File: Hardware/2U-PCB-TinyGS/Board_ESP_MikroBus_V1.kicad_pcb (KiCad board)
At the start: 2 copper layers, 90 x 92 mm, 21 parts, among them J1 Conn_01x19, J2 Conn_01x19, J3 Bus Standard, U1 ESP32-DEVKITC-32D

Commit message: Design changed
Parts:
- removed the 3.3 at (83.2, 21.6)
- removed the G*** at (20.2, 99.9)
- removed the G*** at (82.9, 64.9)
- removed the G*** at (70.2, 51.4) (x2)
- removed the G*** at (82.7, 64.9)
- removed the G*** at (20.2, 100.7)
- added 3.3: Conn_01x02, Connector_PinHeader_2.54mm:PinHeader_1x02_P2.54mm_Vertical, F.Cu at (79.1, 62.9)
- added 3.3: Conn_01x02, Connector_PinHeader_2.54mm:PinHeader_1x02_P2.54mm_Vertical, F.Cu at (86.7, 62.9)
- added 3.3: Conn_01x02, Connector_PinHeader_2.54mm:PinHeader_1x02_P2.54mm_Vertical, F.Cu at (21.1, 63.4)
- added 3.3: Conn_01x02, Connector_PinHeader_2.54mm:PinHeader_1x02_P2.54mm_Vertical, F.Cu at (82.9, 62.9)
- added 3.3: Conn_01x02, Connector_PinHeader_2.54mm:PinHeader_1x02_P2.54mm_Vertical, F.Cu at (29.2, 63.4)
- added 3.3: Conn_01x02, Connector_PinHeader_2.54mm:PinHeader_1x02_P2.54mm_Vertical, F.Cu at (25.4, 63.4)
- added G***: LOGO, Logos-image:QRCode_ThingSat_14.5x14.5, F.Cu at (96.9, 25.8)
- added G***: LOGO, Logos-image:Image-Csug_10x10, F.Cu at (97.4, 95.4)
- added I2C2: Grove, Connector:NS-Tech_Grove_1x04_P2mm_Vertical, F.Cu at (28.9, 81.4)
- added I2C3: Grove, Connector:NS-Tech_Grove_1x04_P2mm_Vertical, F.Cu at (28.9, 89.3)
- added I2C4: Grove, Connector:NS-Tech_Grove_1x04_P2mm_Vertical, F.Cu at (60.1, 81.4)
- added I2C5: Grove, Connector:NS-Tech_Grove_1x04_P2mm_Vertical, F.Cu at (60.1, 73.5)
- added REF**: MountingHole_3.5mm, MountingHole:MountingHole_3.5mm, F.Cu at (21.5, 19.7)
- added REF**: MountingHole_3.5mm, MountingHole:MountingHole_3.5mm, F.Cu at (21.5, 102.2)
- C2: moved to F.Cu
- moved IO_32/33 67.7 mm to (83.2, 92.6)
- moved I2C1 64.3 mm to (28.9, 73.5)
- moved J2 52.5 mm to (73.2, 56.0), turned to -90 degrees
- moved 5V1 47.8 mm to (44.8, 62.2)
- moved J1 47.4 mm to (73.3, 20.4), turned to -90 degrees
- moved UART0 40.8 mm to (60.1, 89.3), turned to 90 degrees
- moved C1 38.9 mm to (24.0, 27.8), turned to -90 degrees
- moved C2 32.9 mm to (22.7, 24.8), turned to 180 degrees
- moved Jmp_Rx1 28.5 mm to (70.7, 100.5)
- moved Jmp_Tx1 26.5 mm to (61.6, 100.5), turned to -90 degrees
- moved U1 15.4 mm to (53.5, 38.2), turned to -90 degrees
- moved MiKroBus_1 10.8 mm to (73.8, 88.1), turned to 180 degrees
- moved MiKroBus_0 10.7 mm to (43.3, 88.1), turned to 180 degrees
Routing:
- net I2C_SDA: track 236.2 -> 126.4 mm, vias 1 -> 2
- net I2C_SCL: track 232.6 -> 142.7 mm, vias 0 -> 1
- net PWM_1: track 112.8 -> 50.9 mm, vias 2 -> 1
- net UART2_Tx: track 116.9 -> 60.4 mm
- net Reset_1: track 59.9 -> 106.4 mm
- net UART0_Tx: track 78.1 -> 36.0 mm, vias 0 -> 1
- net UART0_Rx: track 78.1 -> 36.2 mm
- net AN_0: track 40.5 -> 78.2 mm
- net Reset_0: track 42.2 -> 78.0 mm, vias 0 -> 1
- net /13: track 45.5 -> 77.0 mm, vias 0 -> 1
- net AN_1: track 59.8 -> 90.1 mm
- net PWM_0: track 66.7 -> 93.4 mm, vias 0 -> 2
- net /34: track 90.1 -> 66.0 mm
- net MISO_0: track 81.4 -> 57.3 mm
- net UART2_Rx_grove: track 48.1 -> 25.1 mm, vias 1 -> 0
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- added copper zone on B.Cu, net +3.3V
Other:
- board text added: "TinyGS_2.4GHz_Station"
- board text added: "TinyGS_2U_Board_V1"
- board text removed: "Board_V1"
- board text removed: "Board_V1-2U FORMAT"
- board text removed: "ESP32"
- board text removed: "TinyGs_2.4GHz"

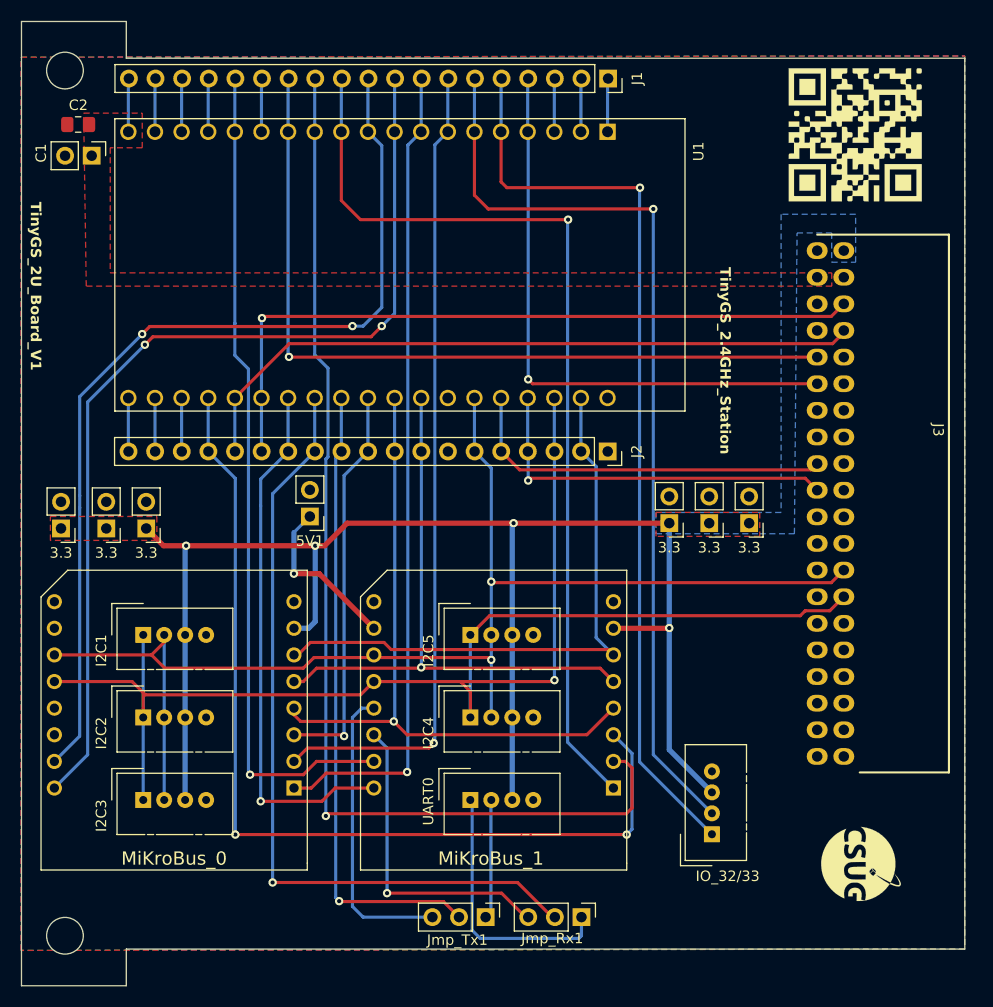
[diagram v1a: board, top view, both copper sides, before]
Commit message: Selection CAN juper added. Can buffer added
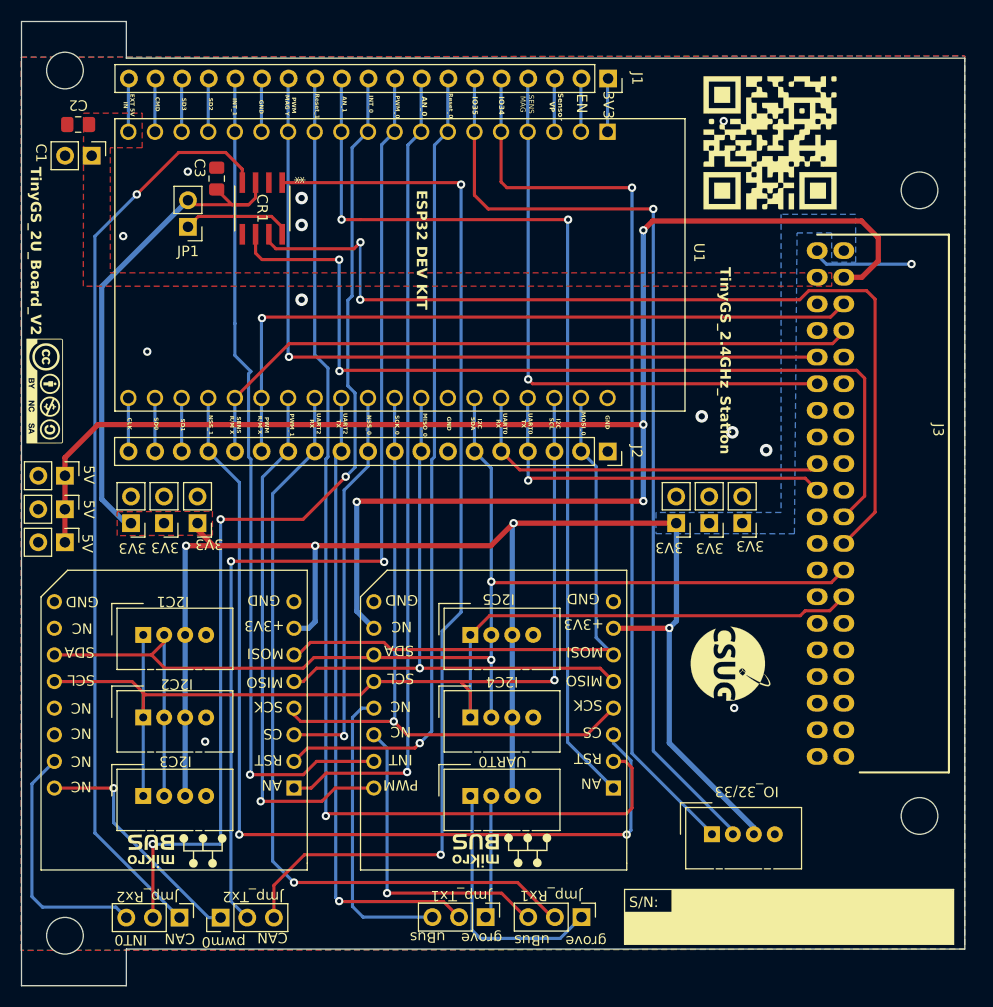
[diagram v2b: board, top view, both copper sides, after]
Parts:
- added 5V1: Conn_01x02, Connector_PinHeader_2.54mm:PinHeader_1x02_P2.54mm_Vertical, F.Cu at (21.5, 58.3)
- added 5V2: Conn_01x02, Connector_PinHeader_2.54mm:PinHeader_1x02_P2.54mm_Vertical, F.Cu at (21.5, 61.5)
- added C3: 100nF, Capacitor_SMD:C_0805_2012Metric_Pad1.18x1.45mm_HandSolder, F.Cu at (35.9, 30.0)
- added CR1: L9616, CAN_buffer:SO-8_STM, F.Cu at (40.3, 32.8)
- added G***: LOGO, Logos-image:mikrobus_logo, F.Cu at (32.4, 94.2)
- added G***: LOGO, Logos-image:mikrobus_logo, F.Cu at (63.4, 94.2)
- added G***: LOGO, Logos-image:license_cc_by_nc_sa, F.Cu at (19.5, 50.3)
- added JP1: Jumper_2_Open, Connector_PinHeader_2.54mm:PinHeader_1x02_P2.54mm_Vertical, F.Cu at (33.2, 34.6)
- added Jmp_Rx2: Jumper_NC_Dual, Connector_PinHeader_2.54mm:PinHeader_1x03_P2.54mm_Vertical, F.Cu at (32.4, 100.5)
- added Jmp_Tx2: Jumper_NC_Dual, Connector_PinHeader_2.54mm:PinHeader_1x03_P2.54mm_Vertical, F.Cu at (36.3, 100.5)
- added REF**: MountingHole_3.5mm, MountingHole:MountingHole_3.5mm, F.Cu at (103.0, 31.1)
- added REF**: MountingHole_3.5mm, MountingHole:MountingHole_3.5mm, F.Cu at (103.0, 90.8)
- moved 5V3 23.5 mm to (21.5, 64.7), turned to -90 degrees
- moved G*** 22.8 mm to (85.0, 76.3)
- moved G*** 8.16 mm to (88.8, 26.5)
- moved 3.1 6.69 mm to (27.8, 62.9)
- moved 3.2 5.53 mm to (30.9, 62.9)
- moved 3.3 4.92 mm to (34.1, 62.9)
- moved 3.4 0.66 mm to (79.8, 62.9)
- moved 3.6 0.66 mm to (86.1, 62.9)
- moved I2C3 0.38 mm to (28.9, 88.9)
- moved UART0 0.38 mm to (60.1, 88.9)
- turned IO_32/33 to 90 degrees
- renumbered 3.3 to 3.1, 3.3 to 3.2, 3.3 to 3.4, 3.3 to 3.5, 3.3 to 3.6, 5V1 to 5V3
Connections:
- J1 pad 10: INT_0 -> ESP_CAN0_RD/INT_0
- J1 pad 9: PWM_0 -> ESP_CAN0_TD/PWM_0
- J3 pad 22: unconnected-(J3-RD-Pad22) -> CAN_RD
- J3 pad 24: unconnected-(J3-TD-Pad24) -> CAN_TD
- J3 pad 4: unconnected-(J3-5V-Pad4) -> +5V
- U1 pad 10: INT_0 -> ESP_CAN0_RD/INT_0
- U1 pad 9: PWM_0 -> ESP_CAN0_TD/PWM_0
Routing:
- net +5V: track 15.9 -> 160.1 mm, vias 1 -> 4
- net CAN0_TD: track 0.00 -> 102.1 mm, vias 0 -> 2
- net ESP_CAN0_RD/INT_0: track 0.00 -> 97.6 mm, vias 0 -> 3
- net ESP_CAN0_TD/PWM_0: track 0.00 -> 96.0 mm, vias 0 -> 2
- net CAN_TD: track 0.00 -> 89.8 mm, vias 0 -> 2
- net CAN0_RD: track 0.00 -> 87.7 mm, vias 0 -> 1
- net CAN_RD: track 0.00 -> 85.2 mm, vias 0 -> 2
- net PWM_0: track 93.4 -> 22.9 mm, vias 2 -> 1
- net INT_0: track 90.6 -> 23.6 mm, vias 2 -> 0
- net +3.3V: track 144.5 -> 196.3 mm
- net Net-(CR1-ASC): track 0.00 -> 10.9 mm
- net GNDREF: track 5.10 -> 14.9 mm, vias 0 -> 13
- net IN35: track 88.7 -> 91.6 mm
- net UART2_Rx: track 76.2 -> 75.0 mm
- net AN_1: track 90.1 -> 91.2 mm, vias 1 -> 2
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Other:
- board text added: "+3V3"
- board text added: "3V3"
- board text added: "5V"
- board text added: "AN"
- board text added: "AN_0"
- board text added: "AN_1"
- board text added: "CAN"
- board text added: "CLK"
- board text added: "CMD"
- board text added: "CS"
- board text added: "EN"
- board text added: "ESP32 DEV KIT"
- board text added: "EXT 5V IN"
- board text added: "GND"
- board text added: "I2C SCL"
- board text added: "I2C SDA"
- board text added: "INT"
- board text added: "INT0"
- board text added: "INT_0"
- board text added: "INT_1"
- board text added: "IO34"
- board text added: "IO35"
- board text added: "MISO"
- board text added: "MISO_0"
- board text added: "MOSI"
- board text added: "MOSI_0"
- board text added: "NC"
- board text added: "NSS_0"
- board text added: "NSS_1"
- board text added: "PWM"
- board text added: "PWM MAG Y"
- board text added: "PWM R/M X"
- board text added: "PWM_0"
- board text added: "PWM_1"
- board text added: "RST"
- board text added: "Reset_0"
- board text added: "Reset_1"
- board text added: "S/N:"
- board text added: "SCK"
- board text added: "SCK_0"
- board text added: "SCL"
- board text added: "SD0"
- board text added: "SD1"
- board text added: "SD2"
- board text added: "SD3"
- board text added: "SDA"
- board text added: "SENS MAG"
- board text added: "SENS R/M X"
- board text added: "Sensor VP"
- board text added: "TinyGS_2U_Board_V2"
- board text added: "UART0 RX"
- board text added: "UART0 TX"
- board text added: "UART2 RX"
- board text added: "UART2 TX"
- board text added: "grove"
- board text added: "pwm0"
- board text added: "uBus"
- board text removed: "TinyGS_2U_Board_V1"

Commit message: Flatsat connector was in the wrong side. All routes were remade.
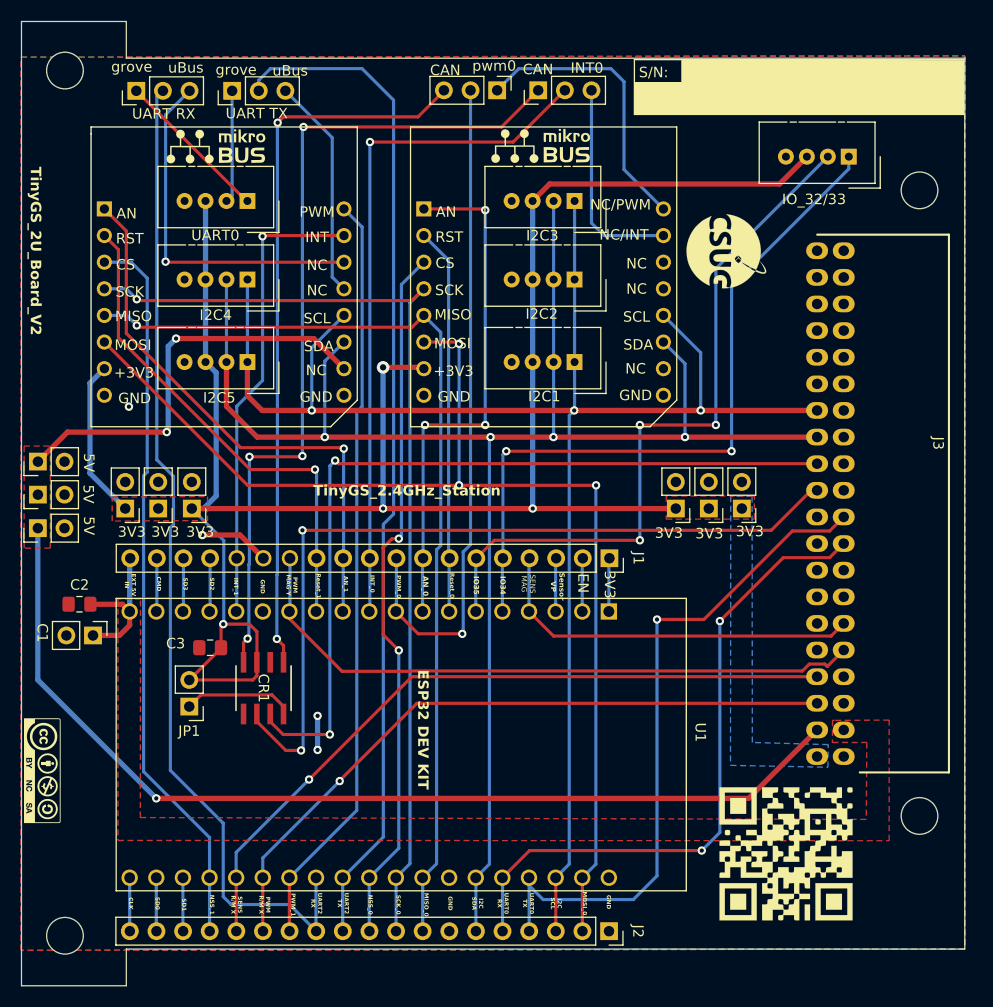
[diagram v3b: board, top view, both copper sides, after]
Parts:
- moved Jmp_Rx1 89.6 mm to (28.3, 21.6), turned to 90 degrees
- moved Jmp_Rx2 86.0 mm to (66.6, 21.6), turned to 90 degrees
- moved Jmp_Tx2 83.2 mm to (62.7, 21.6), turned to -90 degrees
- moved Jmp_Tx1 82.5 mm to (37.4, 21.6), turned to 90 degrees
- moved G*** 75.6 mm to (66.6, 26.8), turned to 0 degrees
- moved MiKroBus_1 73.6 mm to (25.2, 32.9), turned to 0 degrees
- moved G*** 72.8 mm to (35.6, 26.8), turned to 0 degrees
- moved I2C3 70.1 mm to (70.1, 32.1), turned to -90 degrees
- moved G*** 67.9 mm to (90.3, 94.4)
- moved IO_32/33 66.0 mm to (96.2, 27.9), turned to -90 degrees
- moved UART0 60.6 mm to (38.9, 32.1), turned to -90 degrees
- moved I2C2 58.6 mm to (70.1, 39.6), turned to -90 degrees
- moved MiKroBus_0 56.6 mm to (55.7, 32.9), turned to 0 degrees
- moved I2C1 48.7 mm to (70.1, 47.5), turned to -90 degrees
- moved I2C4 46.9 mm to (38.9, 39.6), turned to -90 degrees
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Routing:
- net Reset_1: track 106.4 -> 47.9 mm
- net MOSI_0: track 57.3 -> 112.6 mm, vias 0 -> 3
- net Reset_0: track 77.3 -> 36.9 mm, vias 1 -> 0
- net AN_1: track 91.2 -> 53.6 mm, vias 2 -> 1
- net UART2_Tx: track 60.4 -> 96.9 mm, vias 1 -> 0
- net INT_1: track 79.6 -> 44.6 mm
- net MISO_0: track 57.4 -> 91.6 mm
- net I2C_SDA: track 126.0 -> 159.7 mm, vias 2 -> 4
- net CAN0_TD: track 102.1 -> 69.0 mm
- net ESP_CAN0_RD/INT_0: track 97.6 -> 65.5 mm, vias 3 -> 1
- net ESP_CAN0_TD/PWM_0: track 96.0 -> 64.5 mm, vias 2 -> 1
- net SCK_0: track 63.9 -> 93.8 mm
- net UART0_Tx: track 36.0 -> 65.9 mm
- net NSS_0: track 38.0 -> 67.6 mm, vias 1 -> 2
- net AN_0: track 78.2 -> 50.1 mm, vias 1 -> 3
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- added copper zone on F.Cu, net +5V
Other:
- board text added: "NC/INT"
- board text added: "NC/PWM"
- board text added: "UART RX"
- board text added: "UART TX"
